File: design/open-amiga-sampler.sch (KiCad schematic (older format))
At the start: 14 parts, among them J1 Audio in, J2 DB25_Male, U1 MCP6002-xP, U2 ADC0820CCN

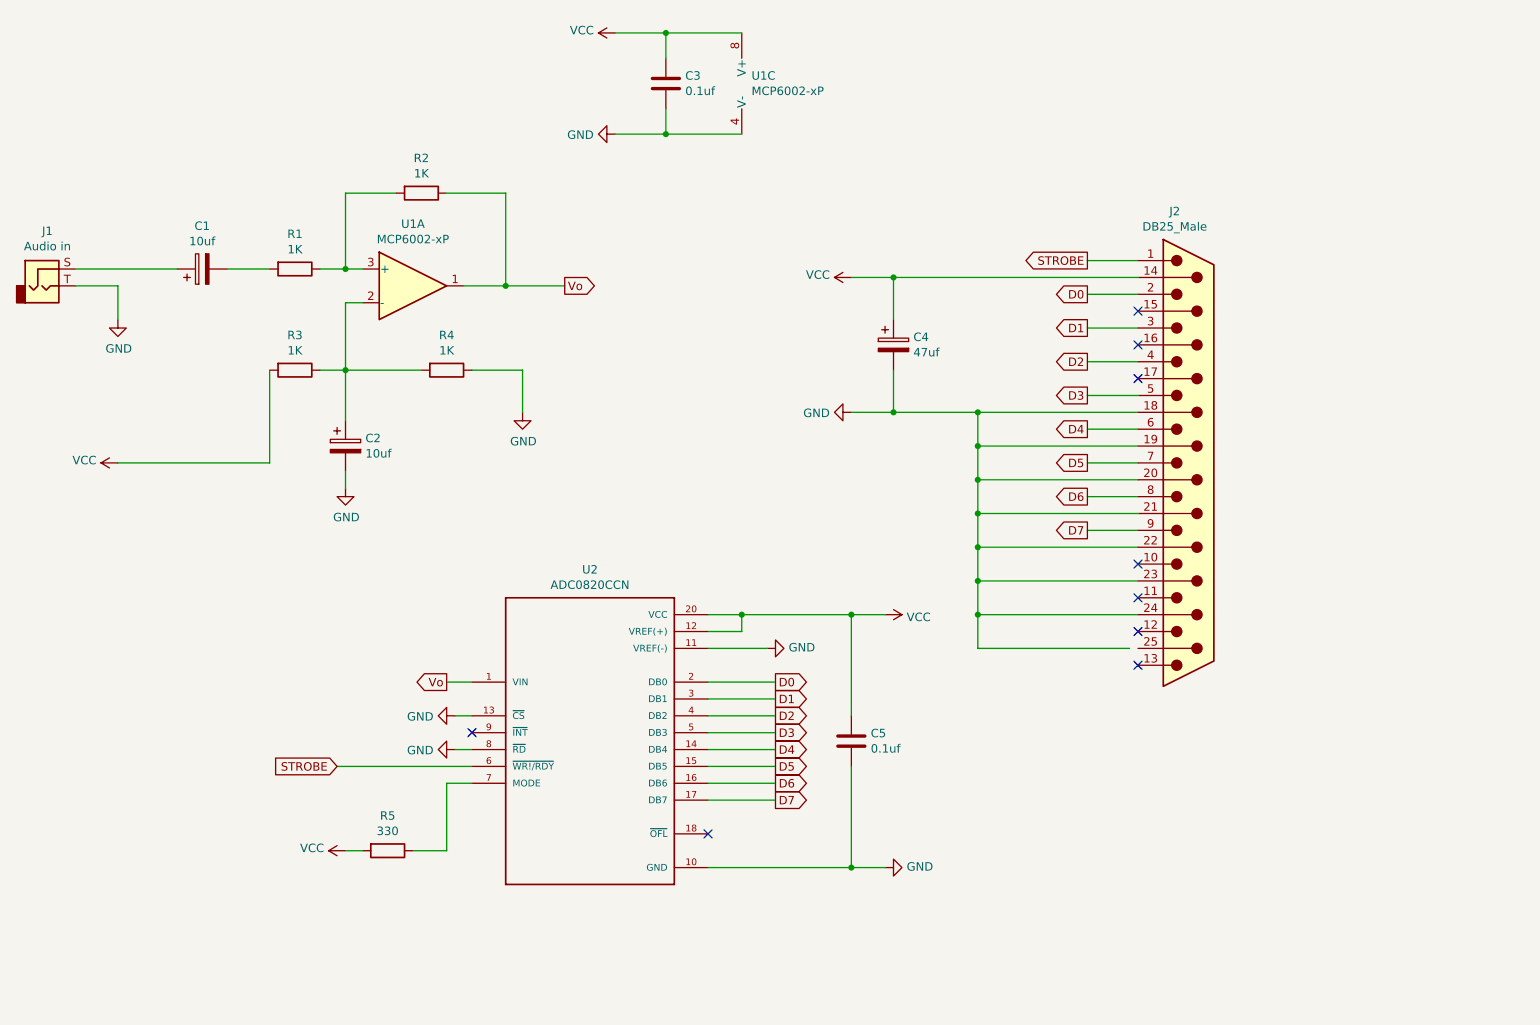
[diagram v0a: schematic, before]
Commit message: Added gain potentiometer
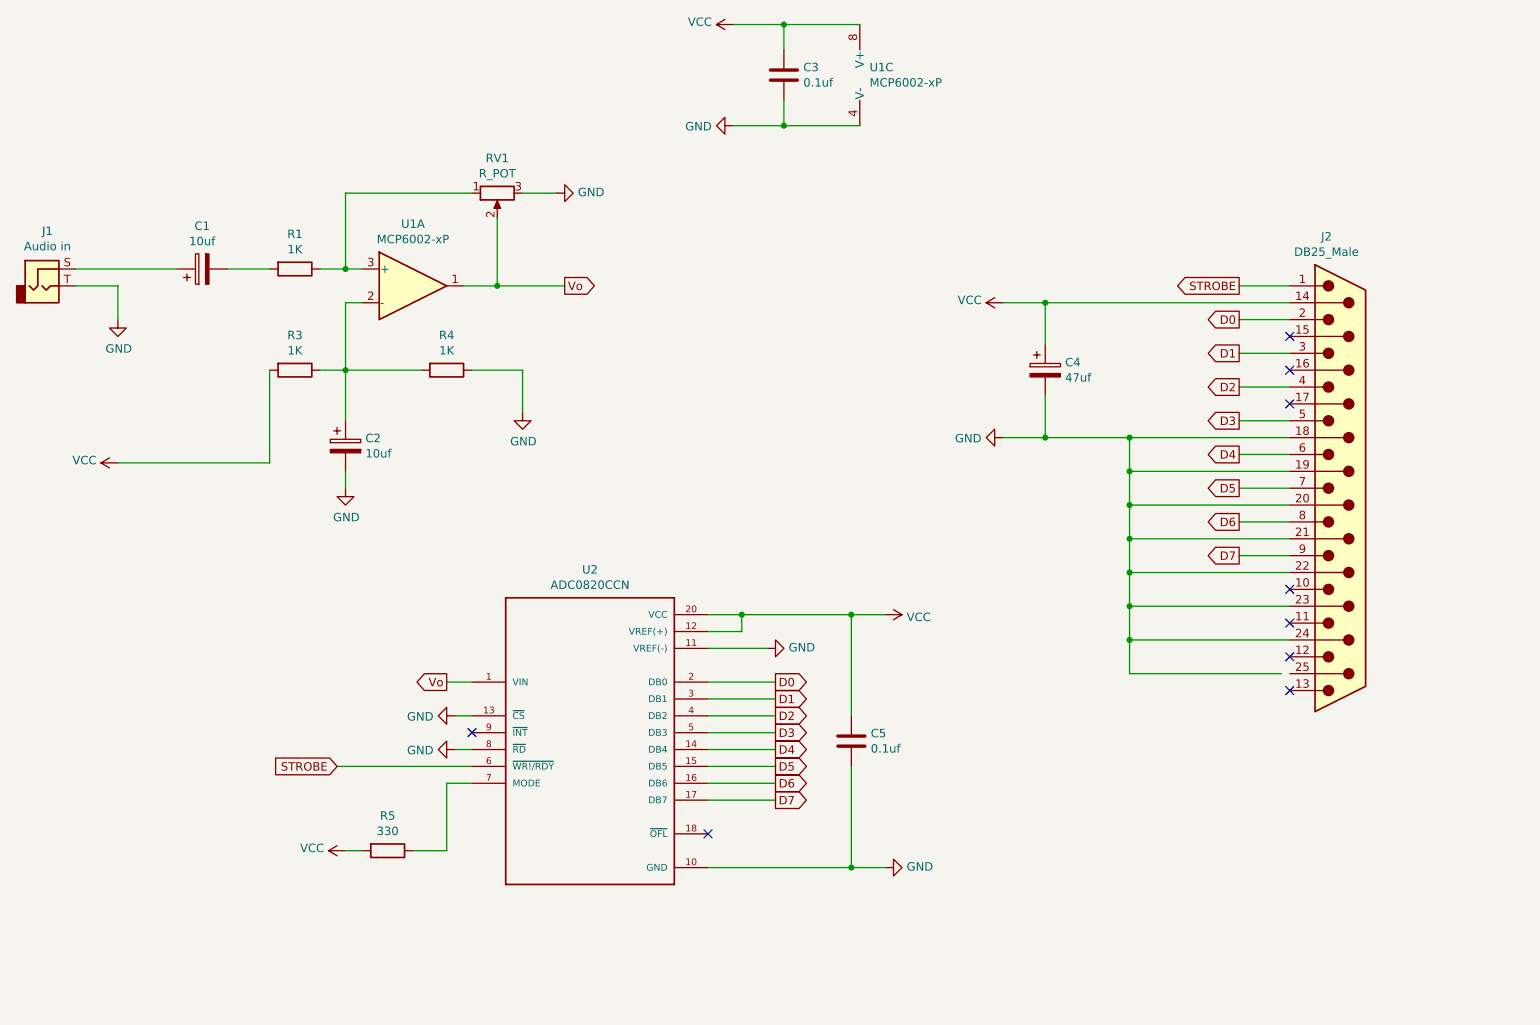
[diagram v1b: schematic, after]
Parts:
- removed R2: 1K, symbol Device:R
- added RV1: R_POT, symbol Device:R_POT
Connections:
- net GND: now also RV1.3
- net Vo: now also RV1.2
- net at R1.1, U1.3 (+): now also RV1.1
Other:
- moved on the sheet: C3, C4, J2, U1C

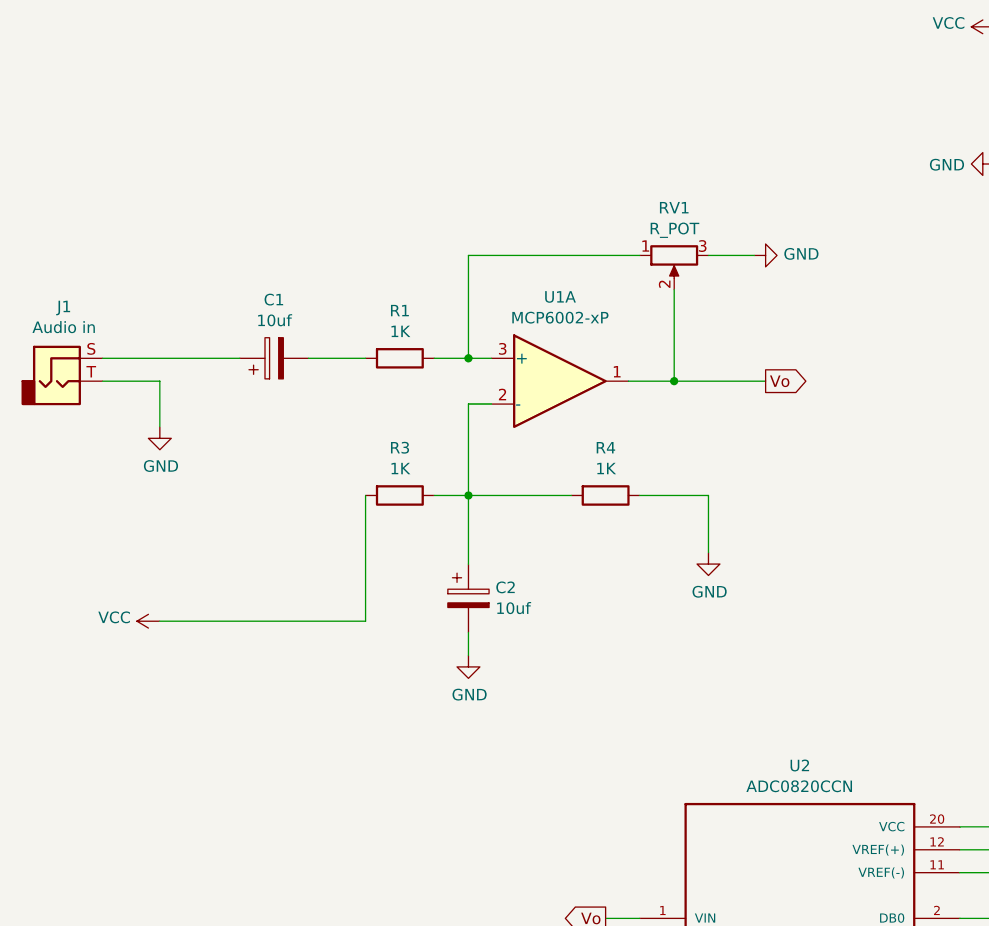
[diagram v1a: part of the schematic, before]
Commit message: Fixed + and - on the op amp being the wrong way
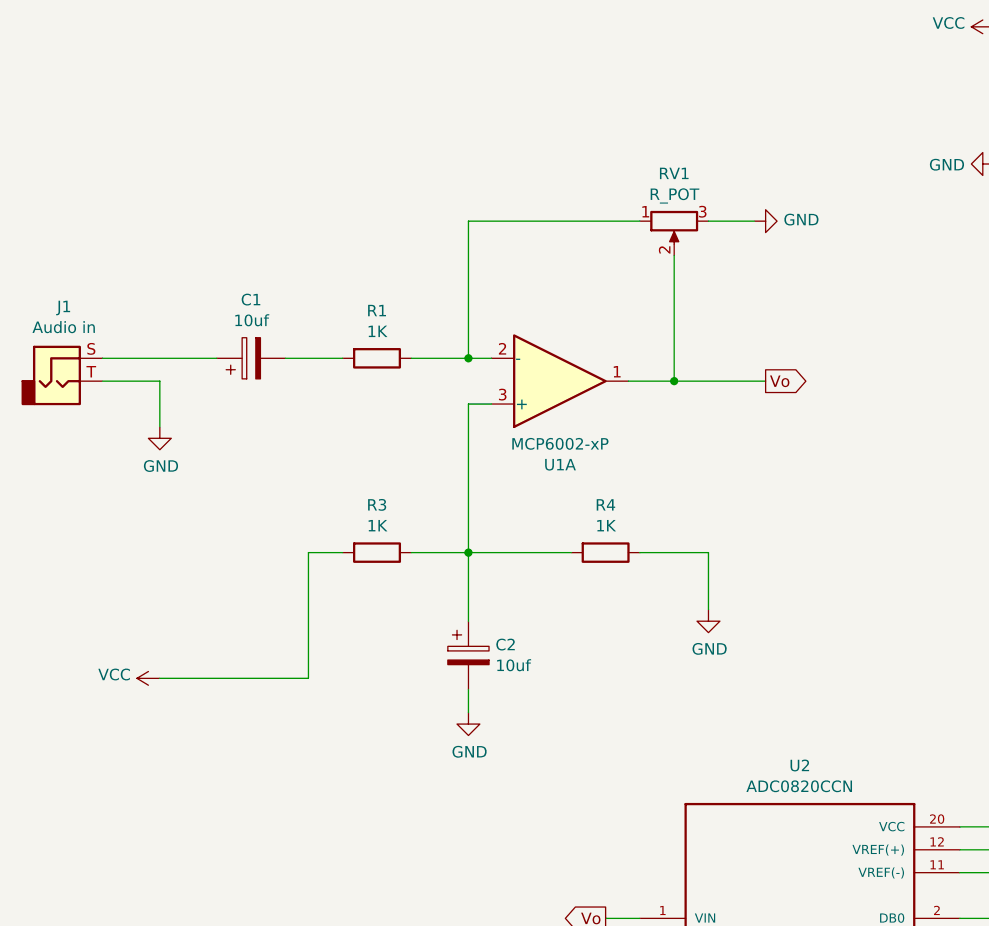
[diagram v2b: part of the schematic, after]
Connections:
- net at C2.1, R3.1, R4.2: now also U1.3 (+); no longer U1.2 (-)
- net at R1.1, RV1.1: now also U1.2 (-); no longer U1.3 (+)
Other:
- moved on the sheet: C1, C2, R1, R3, R4, RV1
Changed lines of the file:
@@
 F 3 "http://ww1.microchip.com/downloads/en/DeviceDoc/21733j.pdf" H 3300 2600 50  0001 C CNN
 	1    3300 2600
-	1    0    0    -1
+	1    0    0    1
 $EndComp
 $Comp
@@
 L power:VCC #PWR?
 U 1 1 5F025A88
-P 1550 3650
-F 0 "#PWR?" H 1550 3500 50  0001 C CNN
-F 1 "VCC" V 1565 3777 50  0000 L CNN
-F 2 "" H 1550 3650 50  0001 C CNN
-F 3 "" H 1550 3650 50  0001 C CNN
-	1    1550 3650
+P 1550 3900
+F 0 "#PWR?" H 1550 3750 50  0001 C CNN
+F 1 "VCC" V 1565 4027 50  0000 L CNN
+F 2 "" H 1550 3900 50  0001 C CNN
+F 3 "" H 1550 3900 50  0001 C CNN
+	1    1550 3900
 	0    -1   -1   0
 $EndComp
@@
 L power:GND #PWR?
 U 1 1 5F0264E7
-P 2900 3800
-F 0 "#PWR?" H 2900 3550 50  0001 C CNN
-F 1 "GND" H 2905 3627 50  0000 C CNN
-F 2 "" H 2900 3800 50  0001 C CNN
-F 3 "" H 2900 3800 50  0001 C CNN
-	1    2900 3800
+P 2900 4050
+F 0 "#PWR?" H 2900 3800 50  0001 C CNN
+F 1 "GND" H 2905 3877 50  0000 C CNN
+F 2 "" H 2900 4050 50  0001 C CNN
+F 3 "" H 2900 4050 50  0001 C CNN
+	1    2900 4050
 	1    0    0    -1
 $EndComp
@@
 L power:GND #PWR?
 U 1 1 5F026AB8
-P 3950 3350
-F 0 "#PWR?" H 3950 3100 50  0001 C CNN
-F 1 "GND" H 3955 3177 50  0000 C CNN
-F 2 "" H 3950 3350 50  0001 C CNN
-F 3 "" H 3950 3350 50  0001 C CNN
-	1    3950 3350
+P 3950 3600
+F 0 "#PWR?" H 3950 3350 50  0001 C CNN
+F 1 "GND" H 3955 3427 50  0000 C CNN
+F 2 "" H 3950 3600 50  0001 C CNN
+F 3 "" H 3950 3600 50  0001 C CNN
+	1    3950 3600
 	1    0    0    -1
 $EndComp
@@
 L Device:CP C1
 U 1 1 5F027226
-P 2050 2500
-F 0 "C1" V 2305 2500 50  0000 C CNN
-F 1 "10uf" V 2214 2500 50  0000 C CNN
-F 2 "" H 2088 2350 50  0001 C CNN
-F 3 "~" H 2050 2500 50  0001 C CNN
-	1    2050 2500
+P 1950 2500
+F 0 "C1" V 2205 2500 50  0000 C CNN
+F 1 "10uf" V 2114 2500 50  0000 C CNN
+F 2 "" H 1988 2350 50  0001 C CNN
+F 3 "~" H 1950 2500 50  0001 C CNN
+	1    1950 2500
 	0    -1   -1   0
 $EndComp
@@
 L Device:CP C2
 U 1 1 5F027977
-P 2900 3550
-F 0 "C2" H 3018 3596 50  0000 L CNN
-F 1 "10uf" H 3018 3505 50  0000 L CNN
-F 2 "" H 2938 3400 50  0001 C CNN
-F 3 "~" H 2900 3550 50  0001 C CNN
-	1    2900 3550
+P 2900 3800
+F 0 "C2" H 3018 3846 50  0000 L CNN
+F 1 "10uf" H 3018 3755 50  0000 L CNN
+F 2 "" H 2938 3650 50  0001 C CNN
+F 3 "~" H 2900 3800 50  0001 C CNN
+	1    2900 3800
 	1    0    0    -1
 $EndComp
@@
 L Device:R R1
 U 1 1 5F02814E
-P 2600 2500
-F 0 "R1" V 2393 2500 50  0000 C CNN
-F 1 "1K" V 2484 2500 50  0000 C CNN
-F 2 "" V 2530 2500 50  0001 C CNN
-F 3 "~" H 2600 2500 50  0001 C CNN
-	1    2600 2500
+P 2500 2500
+F 0 "R1" V 2293 2500 50  0000 C CNN
+F 1 "1K" V 2384 2500 50  0000 C CNN
+F 2 "" V 2430 2500 50  0001 C CNN
+F 3 "~" H 2500 2500 50  0001 C CNN
+	1    2500 2500
 	0    1    1    0
 $EndComp
@@
 L Device:R R3
 U 1 1 5F02BB67
-P 2600 3100
-F 0 "R3" V 2393 3100 50  0000 C CNN
-F 1 "1K" V 2484 3100 50  0000 C CNN
-F 2 "" V 2530 3100 50  0001 C CNN
-F 3 "~" H 2600 3100 50  0001 C CNN
-	1    2600 3100
+P 2500 3350
+F 0 "R3" V 2293 3350 50  0000 C CNN
+F 1 "1K" V 2384 3350 50  0000 C CNN
+F 2 "" V 2430 3350 50  0001 C CNN
+F 3 "~" H 2500 3350 50  0001 C CNN
+	1    2500 3350
 	0    1    1    0
 $EndComp
@@
 L Device:R R4
 U 1 1 5F02BE2F
-P 3500 3100
-F 0 "R4" V 3293 3100 50  0000 C CNN
-F 1 "1K" V 3384 3100 50  0000 C CNN
-F 2 "" V 3430 3100 50  0001 C CNN
-F 3 "~" H 3500 3100 50  0001 C CNN
-	1    3500 3100
+P 3500 3350
+F 0 "R4" V 3293 3350 50  0000 C CNN
+F 1 "1K" V 3384 3350 50  0000 C CNN
+F 2 "" V 3430 3350 50  0001 C CNN
+F 3 "~" H 3500 3350 50  0001 C CNN
+	1    3500 3350
 	0    1    1    0
 $EndComp
@@
 	1550 2600 1550 2800
 Wire Wire Line
-	1300 2500 1900 2500
-Wire Wire Line
-	2200 2500 2450 2500
-Wire Wire Line
-	2750 2500 2900 2500
-Wire Wire Line
-	2900 2050 2900 2500
-Connection ~ 2900 2500
-Wire Wire Line
-	2900 2500 3000 2500
-Wire Wire Line
-	1550 3650 2450 3650
-Wire Wire Line
-	2450 3650 2450 3100
-Wire Wire Line
-	2750 3100 2900 3100
-Wire Wire Line
-	2900 3100 2900 2700
+	1300 2500 1800 2500
+Wire Wire Line
+	2100 2500 2350 2500
+Wire Wire Line
+	1550 3900 2200 3900
+Wire Wire Line
+	2200 3900 2200 3350
+Wire Wire Line
+	2650 3350 2900 3350
 Wire Wire Line
 	2900 2700 3000 2700
 Wire Wire Line
-	2900 3100 3350 3100
-Connection ~ 2900 3100
-Wire Wire Line
-	3650 3100 3950 3100
-Wire Wire Line
-	3950 3100 3950 3350
-Wire Wire Line
-	2900 3100 2900 3400
-Wire Wire Line
-	2900 3700 2900 3800
+	2900 3350 3350 3350
+Connection ~ 2900 3350
+Wire Wire Line
+	3650 3350 3950 3350
+Wire Wire Line
+	3950 3350 3950 3600
+Wire Wire Line
+	2900 3350 2900 3650
+Wire Wire Line
+	2900 3950 2900 4050
 Text GLabel 4200 2600 2    50   Output ~ 0
 Vo
@@
 L Device:R_POT RV1
 U 1 1 5F2122D4
-P 3800 2050
-F 0 "RV1" V 3593 2050 50  0000 C CNN
-F 1 "R_POT" V 3684 2050 50  0000 C CNN
-F 2 "" H 3800 2050 50  0001 C CNN
-F 3 "~" H 3800 2050 50  0001 C CNN
-	1    3800 2050
+P 3800 1900
+F 0 "RV1" V 3593 1900 50  0000 C CNN
+F 1 "R_POT" V 3684 1900 50  0000 C CNN
+F 2 "" H 3800 1900 50  0001 C CNN
+F 3 "~" H 3800 1900 50  0001 C CNN
+	1    3800 1900
 	0    -1   1    0
 $EndComp
@@
 L power:GND #PWR?
 U 1 1 5F218CFB
-P 4150 2050
-F 0 "#PWR?" H 4150 1800 50  0001 C CNN
-F 1 "GND" V 4155 1922 50  0000 R CNN
-F 2 "" H 4150 2050 50  0001 C CNN
-F 3 "" H 4150 2050 50  0001 C CNN
-	1    4150 2050
-	0    -1   -1   0
-$EndComp
-Wire Wire Line
-	3950 2050 4150 2050
-Wire Wire Line
-	3600 2600 3800 2600
-Wire Wire Line
-	2900 2050 3650 2050
-Wire Wire Line
-	3800 2200 3800 2600
-Connection ~ 3800 2600
-Wire Wire Line
-	3800 2600 4200 2600
+P 4150 1900
+F 0 "#PWR?" H 4150 1650 50  0001 C CNN
+F 1 "GND" V 4155 1772 50  0000 R CNN
+F 2 "" H 4150 1900 50  0001 C CNN
+F 3 "" H 4150 1900 50  0001 C CNN
+	1    4150 1900
+	0    -1   -1   0
+$EndComp
+Wire Wire Line
+	3950 1900 4150 1900
+Wire Wire Line
+	2900 1900 3650 1900
 Connection ~ 7050 3500
 Connection ~ 7050 2700
@@
 Wire Wire Line
 	8500 2700 7050 2700
+Wire Wire Line
+	2900 2700 2900 3350
+Wire Wire Line
+	2650 2500 2900 2500
+Wire Wire Line
+	3600 2600 3800 2600
+Wire Wire Line
+	2900 1900 2900 2500
+Connection ~ 2900 2500
+Wire Wire Line
+	2900 2500 3000 2500
+Wire Wire Line
+	3800 2050 3800 2600
+Connection ~ 3800 2600
+Wire Wire Line
+	3800 2600 4200 2600
+Wire Wire Line
+	2200 3350 2350 3350
 $EndSCHEMATC
